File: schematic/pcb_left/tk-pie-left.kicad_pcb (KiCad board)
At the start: 2 copper layers, 150 x 77.5 mm, 36 parts, among them IC1 PCA9539PW,118, J1 NiceView, J2 Battery Connector, J3 Battery Connector, U3 SN74LVC1T45DCK

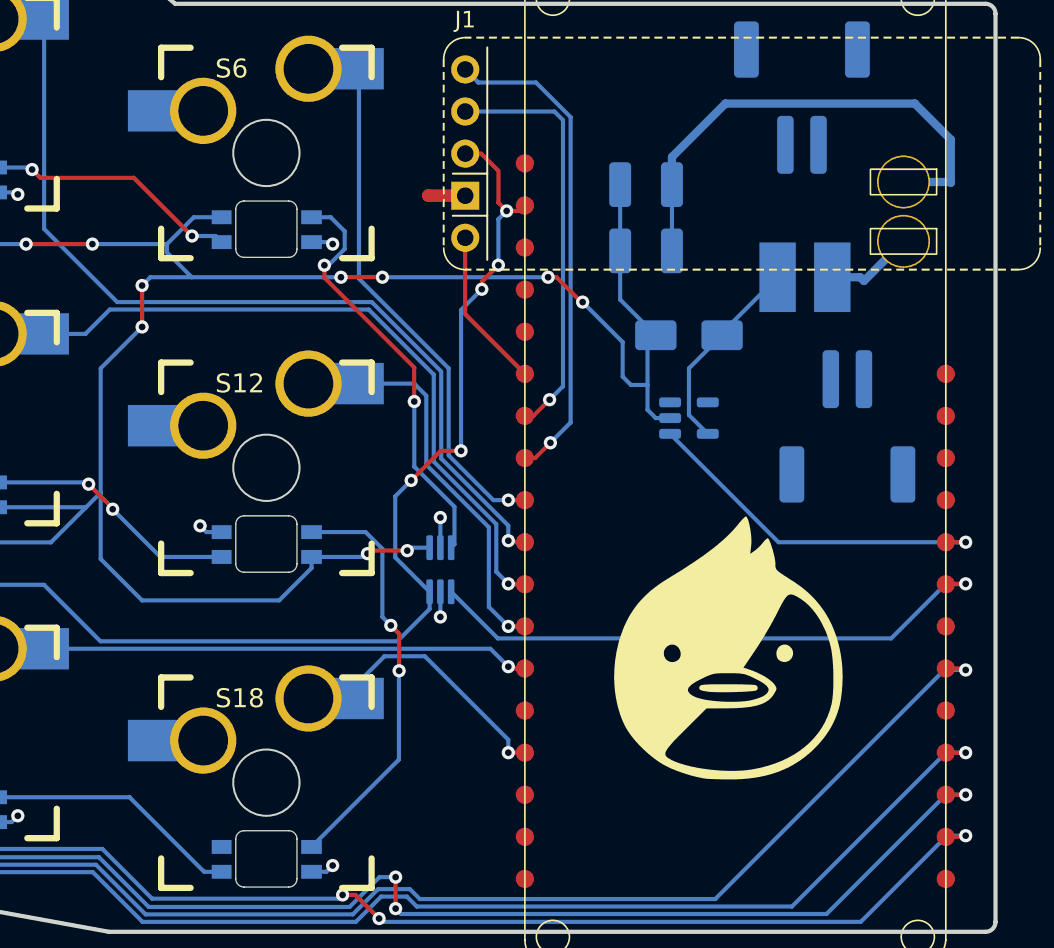
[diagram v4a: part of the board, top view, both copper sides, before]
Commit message: pcb-left: Fix battery traces
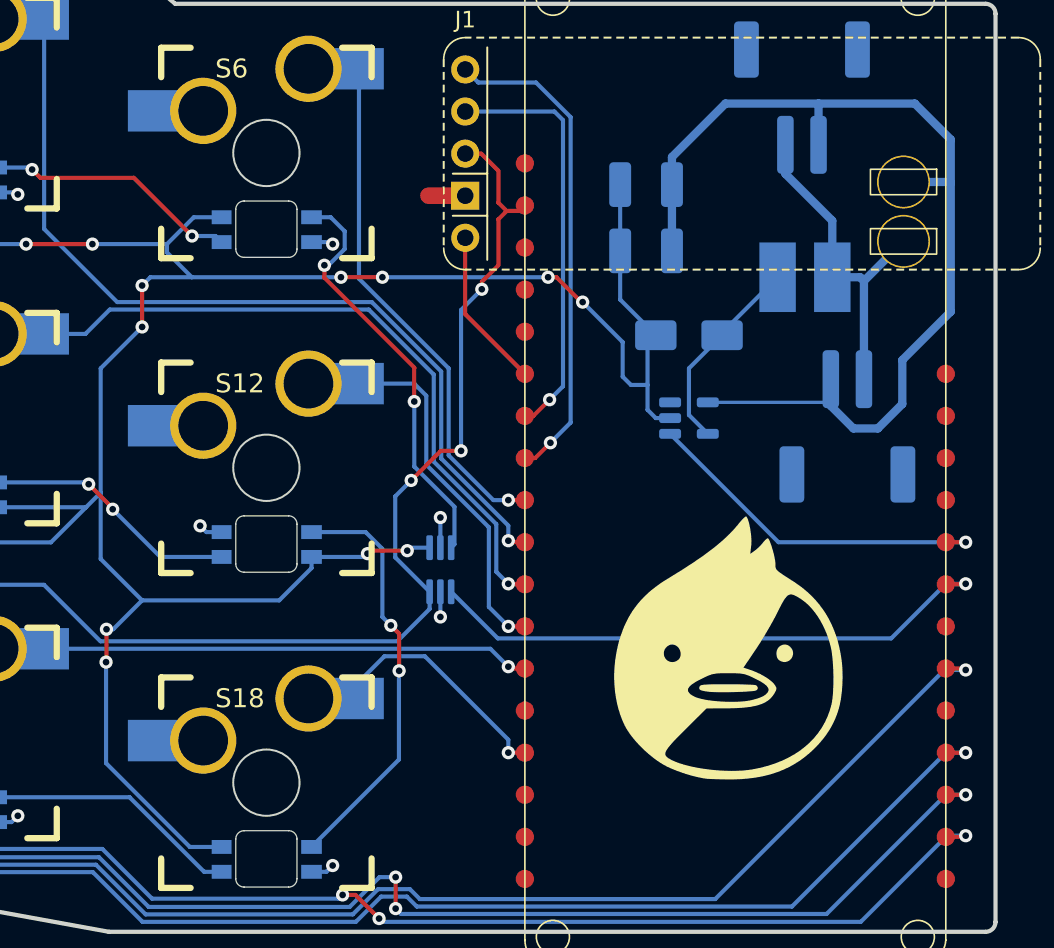
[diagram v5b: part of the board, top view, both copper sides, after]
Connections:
- J2 pad 1: /VBAT -> VBAT+
- J2 pad 2: GND -> VBAT-
- J3 pad 1: /VBAT -> VBAT+
- J3 pad 2: GND -> VBAT-
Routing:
- net VBAT-: track 30.2 -> 63.4 mm
- net +5V: track 488.0 -> 508.0 mm, vias 30 -> 32
- net VBAT+: track 5.38 -> 20.5 mm
- net +3.3V: vias 9 -> 7
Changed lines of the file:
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@@
 	(net 68 "VBAT-")
 	(net 69 "VBAT+")
-	(net 70 "/VBAT")
 	(footprint "Footprints:Pin0.9mm"
 		(layer "F.Cu")
@@
 			(layers "B.Cu" "B.Mask" "B.Paste")
 			(roundrect_rratio 0.25)
-			(net 70 "/VBAT")
+			(net 69 "VBAT+")
 			(pinfunction "Pin_1")
 			(pintype "passive")
@@
 			(layers "B.Cu" "B.Mask" "B.Paste")
 			(roundrect_rratio 0.25)
-			(net 1 "GND")
+			(net 68 "VBAT-")
 			(pinfunction "Pin_2")
 			(pintype "passive")
@@
 			(layers "B.Cu" "B.Mask" "B.Paste")
 			(roundrect_rratio 0.25)
-			(net 70 "/VBAT")
+			(net 69 "VBAT+")
 			(pinfunction "Pin_1")
 			(pintype "passive")
@@
 			(layers "B.Cu" "B.Mask" "B.Paste")
 			(roundrect_rratio 0.25)
-			(net 1 "GND")
+			(net 68 "VBAT-")
 			(pinfunction "Pin_2")
 			(pintype "passive")
@@
 	)
 	(segment
-		(start 121.78 38.58)
-		(end 121.76 38.56)
-		(width 0.75)
-		(layer "F.Cu")
-		(net 1)
-	)
-	(segment
 		(start 124 38.58)
 		(end 121.78 38.58)
-		(width 0.75)
+		(width 1)
 		(layer "F.Cu")
 		(net 1)
@@
 	)
 	(segment
+		(start 102.35 66.7)
+		(end 102.325 66.725)
+		(width 0.25)
+		(layer "F.Cu")
+		(net 3)
+	)
+	(segment
 		(start 129 43.5)
 		(end 129.5 43.5)
@@
 	)
 	(segment
+		(start 102.35 64.744)
+		(end 102.35 66.7)
+		(width 0.25)
+		(layer "F.Cu")
+		(net 3)
+	)
+	(segment
 		(start 80.5 80.125)
 		(end 82.78 77.845)
@@
 	)
 	(via
+		(at 102.325 66.725)
+		(size 0.8)
+		(drill 0.4)
+		(layers "F.Cu" "B.Cu")
+		(net 3)
+	)
+	(via
 		(at 27 67.97)
 		(size 0.8)
@@
 	)
 	(via
+		(at 102.35 64.744)
+		(size 0.8)
+		(drill 0.4)
+		(layers "F.Cu" "B.Cu")
+		(net 3)
+	)
+	(via
 		(at 61.5 59.5)
 		(size 0.8)
@@
 	)
 	(segment
+		(start 107.381414 77.88)
+		(end 109.3 77.88)
+		(width 0.25)
+		(layer "B.Cu")
+		(net 3)
+	)
+	(segment
 		(start 69.5 37.5)
 		(end 65.5 37.5)
@@
 	)
 	(segment
+		(start 102.325 72.823586)
+		(end 107.381414 77.88)
+		(width 0.25)
+		(layer "B.Cu")
+		(net 3)
+	)
+	(segment
 		(start 135 47.5)
 		(end 135 50)
@@
 	)
 	(segment
+		(start 104.5 63)
+		(end 102.756 64.744)
+		(width 0.25)
+		(layer "B.Cu")
+		(net 3)
+	)
+	(segment
 		(start 27 76.5)
 		(end 31.38 80.88)
@@
 	)
 	(segment
+		(start 102.325 66.725)
+		(end 102.325 72.823586)
+		(width 0.25)
+		(layer "B.Cu")
+		(net 3)
+	)
+	(segment
 		(start 97.5 41.5)
 		(end 88 41.5)
@@
 	)
 	(segment
+		(start 102.756 64.744)
+		(end 102.35 64.744)
+		(width 0.25)
+		(layer "B.Cu")
+		(net 3)
+	)
+	(segment
 		(start 50.5 40.5)
 		(end 44.5 46.5)
@@
 	)
 	(segment
+		(start 126 40)
+		(end 126.5 39.5)
+		(width 0.25)
+		(layer "F.Cu")
+		(net 53)
+	)
+	(segment
 		(start 120.737347 55.762653)
 		(end 122.523351 53.976649)
@@
 	)
 	(segment
+		(start 126 42.775)
+		(end 126 40)
+		(width 0.25)
+		(layer "F.Cu")
+		(net 53)
+	)
+	(segment
 		(start 83.825 75.806)
 		(end 83.231 76.4)
@@
 	)
 	(via
-		(at 126 42.775)
-		(size 0.8)
-		(drill 0.4)
-		(layers "F.Cu" "B.Cu")
-		(net 53)
-	)
-	(via
 		(at 81.58 80.14)
 		(size 0.8)
@@
 	)
 	(via
-		(at 126.5 39.5)
-		(size 0.8)
-		(drill 0.4)
-		(layers "F.Cu" "B.Cu")
-		(net 53)
-	)
-	(via
 		(at 75.61 86.37)
 		(size 0.8)
@@
 	)
 	(segment
-		(start 126 42.775)
-		(end 126 40)
-		(width 0.25)
-		(layer "B.Cu")
-		(net 53)
-	)
-	(segment
 		(start 71.876 84)
 		(end 73.32 84)
@@
 	)
 	(segment
-		(start 126 40)
-		(end 126.5 39.5)
-		(width 0.25)
-		(layer "B.Cu")
-		(net 53)
-	)
-	(segment
 		(start 76.352 83.985321)
 		(end 79.347321 80.99)
@@
 	)
 	(segment
+		(start 146.06 49.65)
+		(end 146.06 48.165)
+		(width 0.25)
+		(layer "B.Cu")
+		(net 68)
+	)
+	(segment
+		(start 139.7 33.02)
+		(end 145.325 33.02)
+		(width 0.5)
+		(layer "B.Cu")
+		(net 68)
+	)
+	(segment
 		(start 153.2515 37.7515)
 		(end 153.3 37.8)
@@
 	)
 	(segment
+		(start 148.9 52.625)
+		(end 150.375 51.15)
+		(width 0.5)
+		(layer "B.Cu")
+		(net 68)
+	)
+	(segment
+		(start 145.32 33.025)
+		(end 145.325 33.02)
+		(width 0.2)
+		(layer "B.Cu")
+		(net 68)
+	)
+	(segment
+		(start 153.3 37.8)
+		(end 153.3 45.575)
+		(width 0.5)
+		(layer "B.Cu")
+		(net 68)
+	)
+	(segment
+		(start 138.6375 51.05)
+		(end 145.85 51.05)
+		(width 0.2)
+		(layer "B.Cu")
+		(net 68)
+	)
+	(segment
+		(start 146.06 51.26)
+		(end 147.425 52.625)
+		(width 0.5)
+		(layer "B.Cu")
+		(net 68)
+	)
+	(segment
+		(start 145.32 35.51)
+		(end 145.32 33.025)
+		(width 0.5)
+		(layer "B.Cu")
+		(net 68)
+	)
+	(segment
 		(start 136.475 37.91)
 		(end 136.475 41.91)
-		(width 0.25)
+		(width 0.5)
 		(layer "B.Cu")
 		(net 68)
@@
 	)
 	(segment
-		(start 139.7 33.02)
+		(start 153.3 45.575)
+		(end 150.375 48.5)
+		(width 0.5)
+		(layer "B.Cu")
+		(net 68)
+	)
+	(segment
+		(start 147.425 52.625)
+		(end 148.9 52.625)
+		(width 0.5)
+		(layer "B.Cu")
+		(net 68)
+	)
+	(segment
+		(start 145.85 51.05)
+		(end 146.06 51.26)
+		(width 0.2)
+		(layer "B.Cu")
+		(net 68)
+	)
+	(segment
+		(start 150.375 51.15)
+		(end 150.375 48.5)
+		(width 0.5)
+		(layer "B.Cu")
+		(net 68)
+	)
+	(segment
+		(start 146.06 49.65)
+		(end 146.06 51.26)
+		(width 0.5)
+		(layer "B.Cu")
+		(net 68)
+	)
+	(segment
+		(start 145.325 33.02)
 		(end 151.13 33.02)
 		(width 0.5)
@@
 	)
 	(segment
+		(start 148.06 49.65)
+		(end 148.06 43.726)
+		(width 0.5)
+		(layer "B.Cu")
+		(net 69)
+	)
+	(segment
+		(start 143.32 37.26)
+		(end 146.15 40.09)
+		(width 0.5)
+		(layer "B.Cu")
+		(net 69)
+	)
+	(segment
+		(start 143.32 35.51)
+		(end 143.32 37.26)
+		(width 0.5)
+		(layer "B.Cu")
+		(net 69)
+	)
+	(segment
 		(start 147.834 43.5)
 		(end 146.15 43.5)
@@
 		(width 0.5)
 		(layer "B.Cu")
+		(net 69)
+	)
+	(segment
+		(start 146.15 40.09)
+		(end 146.15 43.5)
+		(width 0.5)
+		(layer "B.Cu")

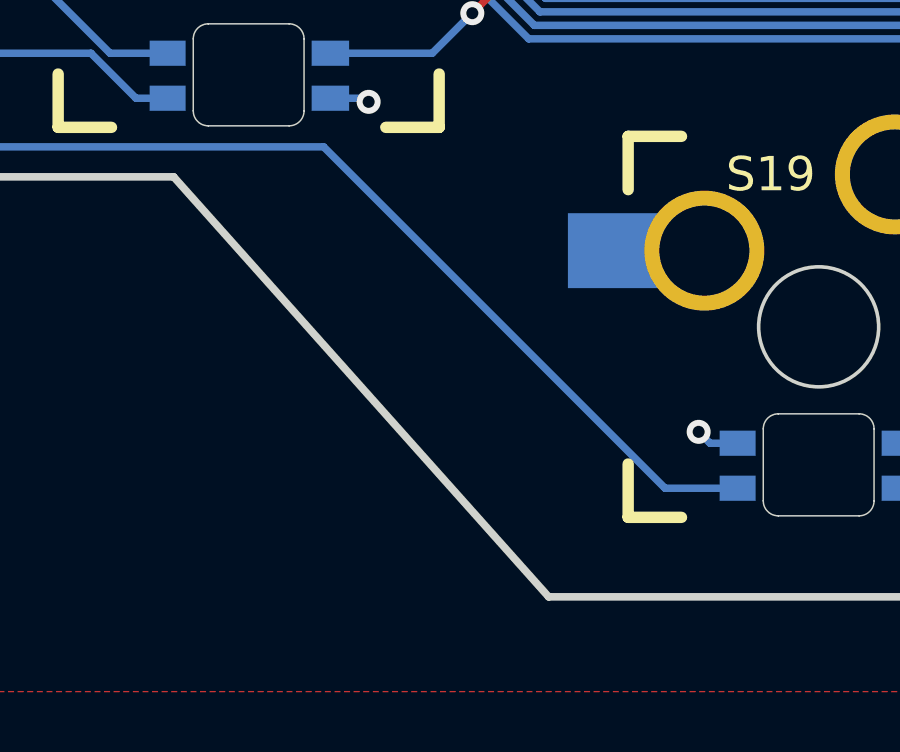
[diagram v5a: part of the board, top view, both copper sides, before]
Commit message: pcb-left: Add name and revision
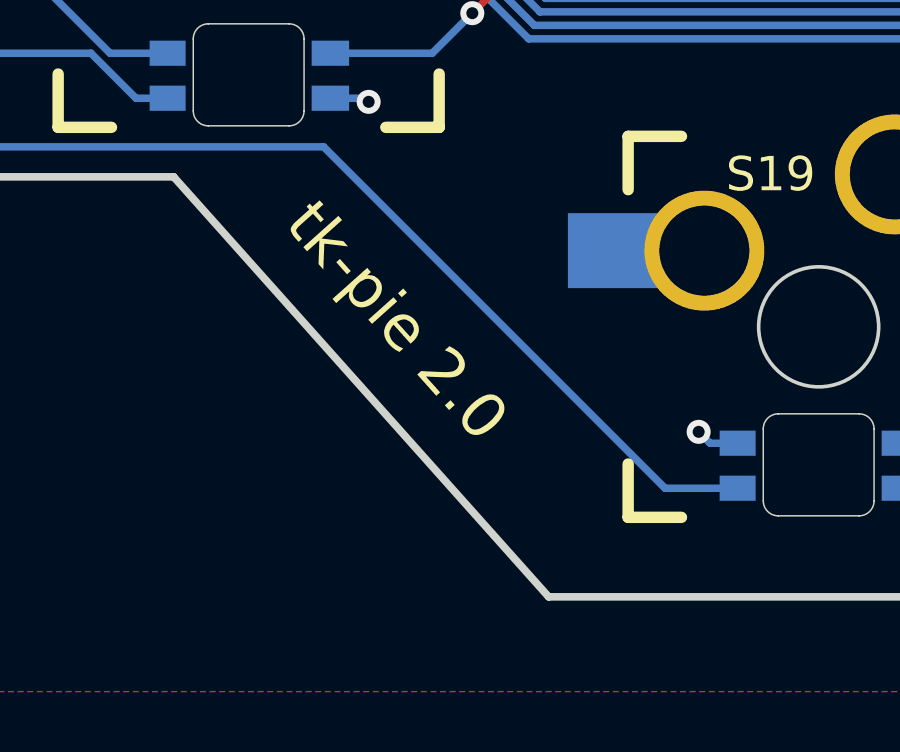
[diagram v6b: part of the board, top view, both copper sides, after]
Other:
- board text added: "tk-pie 2.0"
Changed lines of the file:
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@@
 	)
 	(paper "A5")
+	(title_block
+		(title "tk-pie-left")
+		(date "2025-11-09")
+		(rev "2.0")
+	)
 	(layers
 		(0 "F.Cu" signal)
@@
 		)
 	)
+	(gr_text "tk-pie 2.0"
+		(at 37.025 86.725 311.801)
+		(layer "F.SilkS")
+		(effects
+			(font
+				(size 1.5 1.5)
+				(thickness 0.1875)
+			)
+			(justify left bottom)
+		)
+	)
